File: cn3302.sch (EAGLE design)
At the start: 14 parts, among them M1 CN3302, M2 8m, T1 3.8

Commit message: исправил схему
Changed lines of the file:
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@@
 <setting verticaltext="up"/>
 </settings>
-<grid distance="0.1" unitdist="inch" unit="inch" style="lines" multiple="1" display="yes" altdistance="0.01" altunitdist="inch" altunit="inch"/>
+<grid distance="0.1" unitdist="inch" unit="inch" style="lines" multiple="1" display="no" altdistance="0.01" altunitdist="inch" altunit="inch"/>
 <layers>
 <layer number="1" name="Top" color="4" fill="1" visible="no" active="no"/>
@@
 </segment>
 </net>
-<net name="N$7" class="0">
-<segment>
-<pinref part="M2" gate="G$1" pin="G"/>
-<pinref part="M1" gate="CN3302" pin="HDRV"/>
-<wire x1="-2.54" y1="20.32" x2="15.24" y2="20.32" width="0.1524" layer="91"/>
-<wire x1="15.24" y1="20.32" x2="15.24" y2="10.16" width="0.1524" layer="91"/>
-</segment>
-</net>
 <net name="N$8" class="0">
 <segment>
@@
 </segment>
 </net>
+<net name="N$3" class="0">
+<segment>
+<pinref part="M2" gate="G$1" pin="G"/>
+<wire x1="-2.54" y1="20.32" x2="-2.54" y2="17.78" width="0.1524" layer="91"/>
+<wire x1="-2.54" y1="17.78" x2="17.78" y2="17.78" width="0.1524" layer="91"/>
+<wire x1="17.78" y1="17.78" x2="17.78" y2="10.16" width="0.1524" layer="91"/>
+<pinref part="M1" gate="CN3302" pin="HDRV"/>
+<wire x1="17.78" y1="10.16" x2="15.24" y2="10.16" width="0.1524" layer="91"/>
+</segment>
+</net>

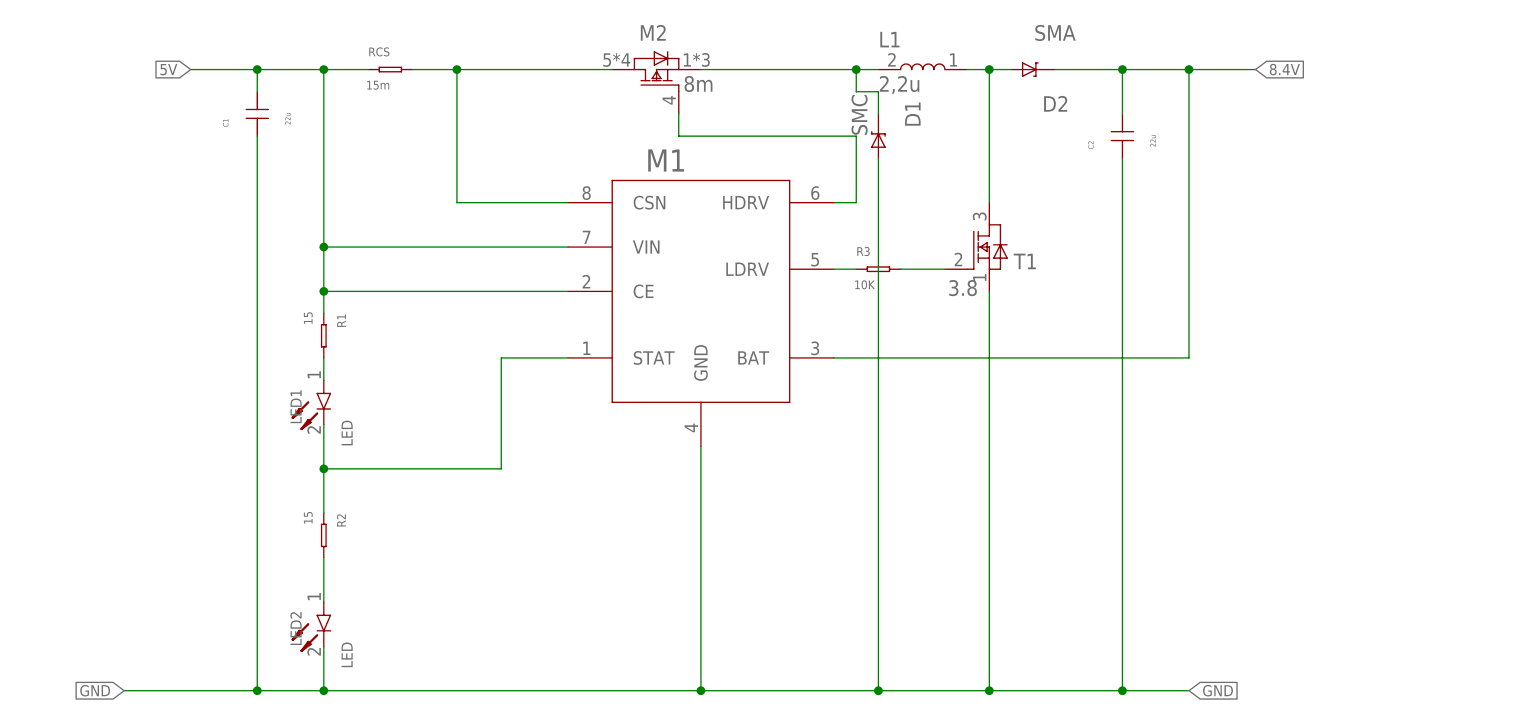
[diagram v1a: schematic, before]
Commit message: отредачил схем
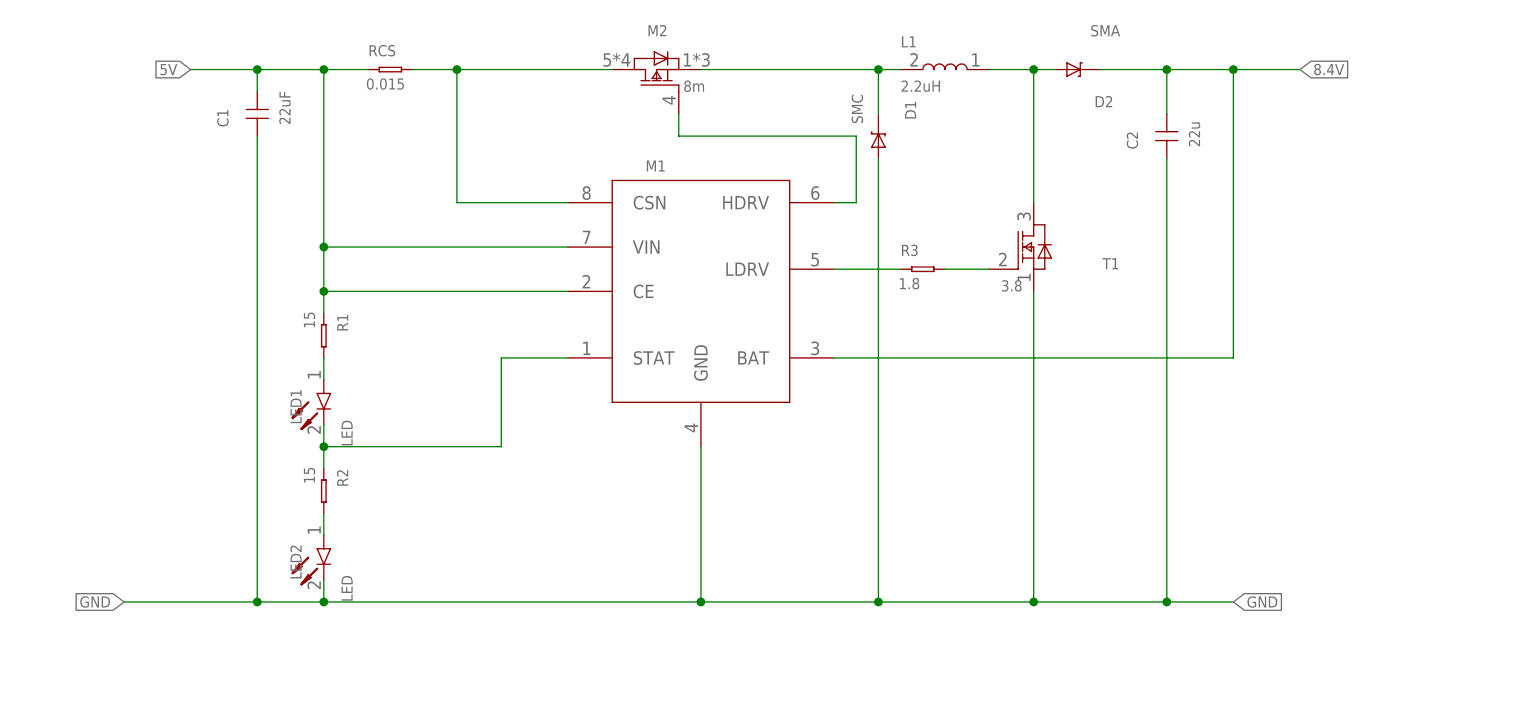
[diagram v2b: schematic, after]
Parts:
- C1: value 22u -> 22uF
- L1: value 2,2u -> 2.2uH
- R3: value 10K -> 1.8
- RCS: value 15m -> 0.015
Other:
- moved on the sheet: C2, D2, L1, LED2, R2, R3, T1

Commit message: Исправил схему
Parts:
- removed M2: 8m, 1_TRANSISTORS:HY15P03S
- removed T1: 3.8, 1_TRANSISTORS:AOD9N50
- added C3, C4, C5, C6, C7, C8: 22uF, 1_RESISTORS:CAPACITOR
- added VT1: HY15P03S, 1_TRANSISTORS:HY15P03S
- added VT2: AOD9N50, 1_TRANSISTORS:AOD9N50
- C2: value 22u -> 22uF
- R1, R2: value 15 -> 500
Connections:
- net 5V: now also C3.P$2, C4.P$2, C5.P$2
- net 8.4V: now also C6.P$2, C7.P$2, C8.P$2
- net GND: now also C3.P$1, C4.P$1, C5.P$1, C6.P$1, C7.P$1, C8.P$1, VT2.S; no longer T1.S
- net N$10: now also VT2.D; no longer T1.D
- net N$3: now also VT1.G; no longer M2.G
- net N$6: now also VT1.S; no longer M2.D
- net N$8: now also VT2.G; no longer T1.G
- net N$9: now also VT1.D; no longer M2.S
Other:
- moved on the sheet: C2, D1, D2, L1, LED1, LED2, R1, R2, R3, RCS
